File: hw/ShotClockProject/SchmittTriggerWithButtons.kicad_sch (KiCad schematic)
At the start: 10 parts, among them SW3 TK-6580S-2, SW4 TK-6580S-2, SW5 TK-6580S-2, U3 M74HC14YRM13TR

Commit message: Finished routing and added silk + part nmbr
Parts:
- C4: LCSC Part # C1525 -> (none)
- R31, R32, R33: LCSC Part # C25744 -> (none)
- SW3, SW4, SW5: LCSC Part # C528775 -> (none)
- U3: LCSC Part # C157450 -> (none)
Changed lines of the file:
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@@
       (effects (font (size 1.27 1.27)) (justify bottom) hide)
     )
-    (property "LCSC Part #" "C157450" (at 176.53 85.09 0)
+    (property "LCSC Part #" "" (at 176.53 85.09 0)
       (effects (font (size 1.27 1.27)) hide)
     )
@@
       (effects (font (size 1.27 1.27)) hide)
     )
-    (property "LCSC Part #" "C1525" (at 138.43 85.09 0)
+    (property "LCSC Part #" "" (at 138.43 85.09 0)
       (effects (font (size 1.27 1.27)) hide)
     )
@@
       (effects (font (size 1.27 1.27)) hide)
     )
-    (property "LCSC Part #" "C528775" (at 104.14 69.85 0)
+    (property "LCSC Part #" "" (at 104.14 69.85 0)
       (effects (font (size 1.27 1.27)) hide)
     )
@@
       (effects (font (size 1.27 1.27)) hide)
     )
-    (property "LCSC Part #" "C25744" (at 113.03 106.68 0)
+    (property "LCSC Part #" "" (at 113.03 106.68 0)
       (effects (font (size 1.27 1.27)) hide)
     )
@@
       (effects (font (size 1.27 1.27)) hide)
     )
-    (property "LCSC Part #" "C1525" (at 138.43 130.81 0)
+    (property "LCSC Part #" "" (at 138.43 130.81 0)
       (effects (font (size 1.27 1.27)) hide)
     )
@@
       (effects (font (size 1.27 1.27)) hide)
     )
-    (property "LCSC Part #" "C25744" (at 113.03 82.55 0)
+    (property "LCSC Part #" "" (at 113.03 82.55 0)
       (effects (font (size 1.27 1.27)) hide)
     )
@@
       (effects (font (size 1.27 1.27)) hide)
     )
-    (property "LCSC Part #" "C528775" (at 104.14 92.71 0)
+    (property "LCSC Part #" "" (at 104.14 92.71 0)
       (effects (font (size 1.27 1.27)) hide)
     )
@@
       (effects (font (size 1.27 1.27)) hide)
     )
-    (property "LCSC Part #" "C1525" (at 138.43 107.95 0)
+    (property "LCSC Part #" "" (at 138.43 107.95 0)
       (effects (font (size 1.27 1.27)) hide)
     )
@@
       (effects (font (size 1.27 1.27)) hide)
     )
-    (property "LCSC Part #" "C25744" (at 113.03 128.27 0)
+    (property "LCSC Part #" "" (at 113.03 128.27 0)
       (effects (font (size 1.27 1.27)) hide)
     )
@@
       (effects (font (size 1.27 1.27)) hide)
     )
-    (property "LCSC Part #" "C528775" (at 104.14 115.57 0)
-      (effects (font (size 1.27 1.27)) hide)
-    )
+    (property "LCSC Part #" "" (at 104.14 115.57 0)
+      (effects (font (size 1.27 1.27)) hide)
+    )

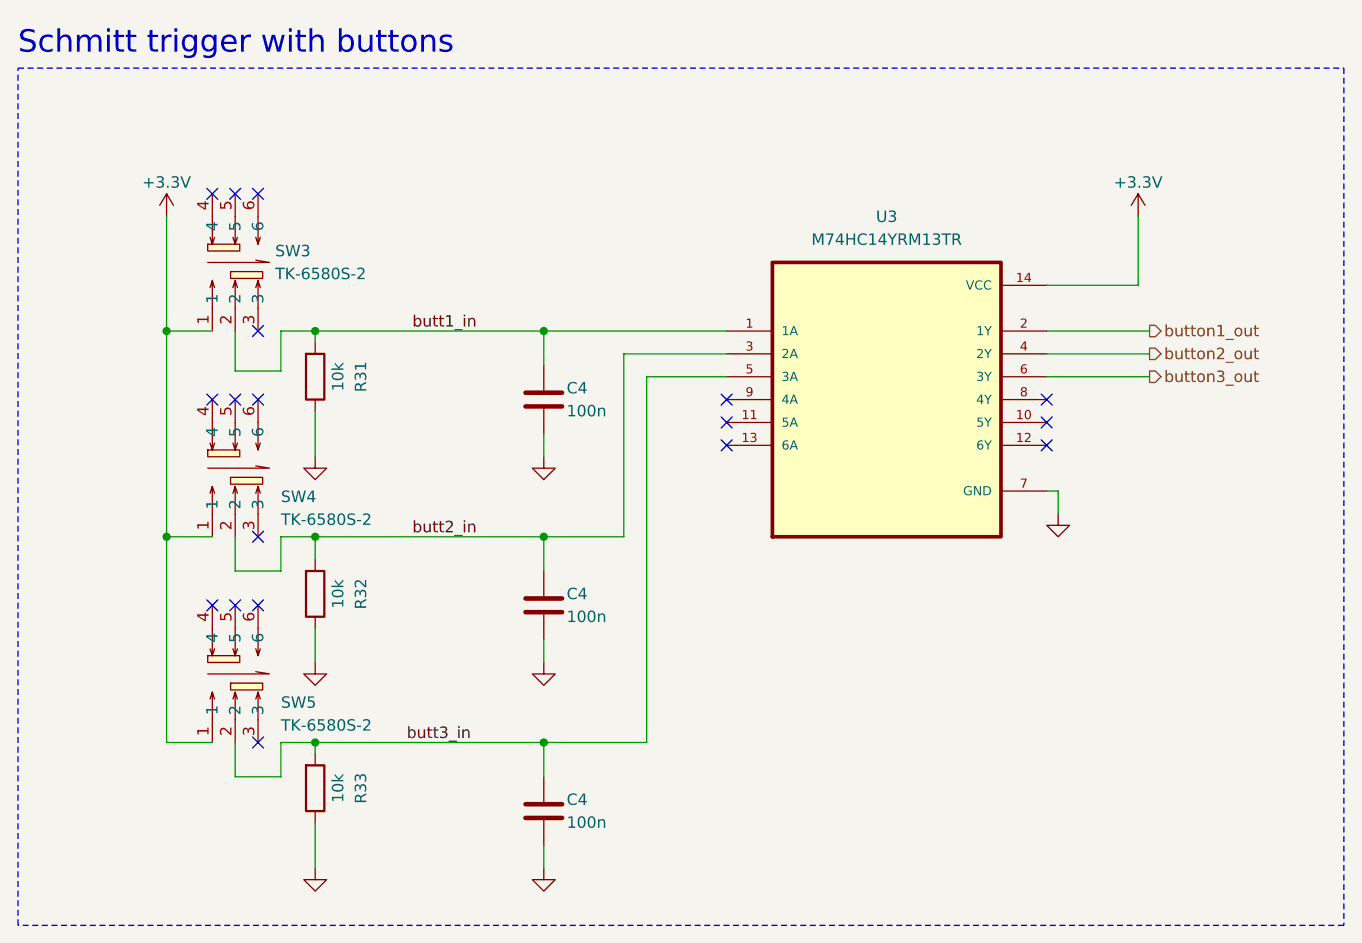
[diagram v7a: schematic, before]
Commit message: Add REV3 odt file, update CubeMX version and fix the ADC readout for battery voltage.
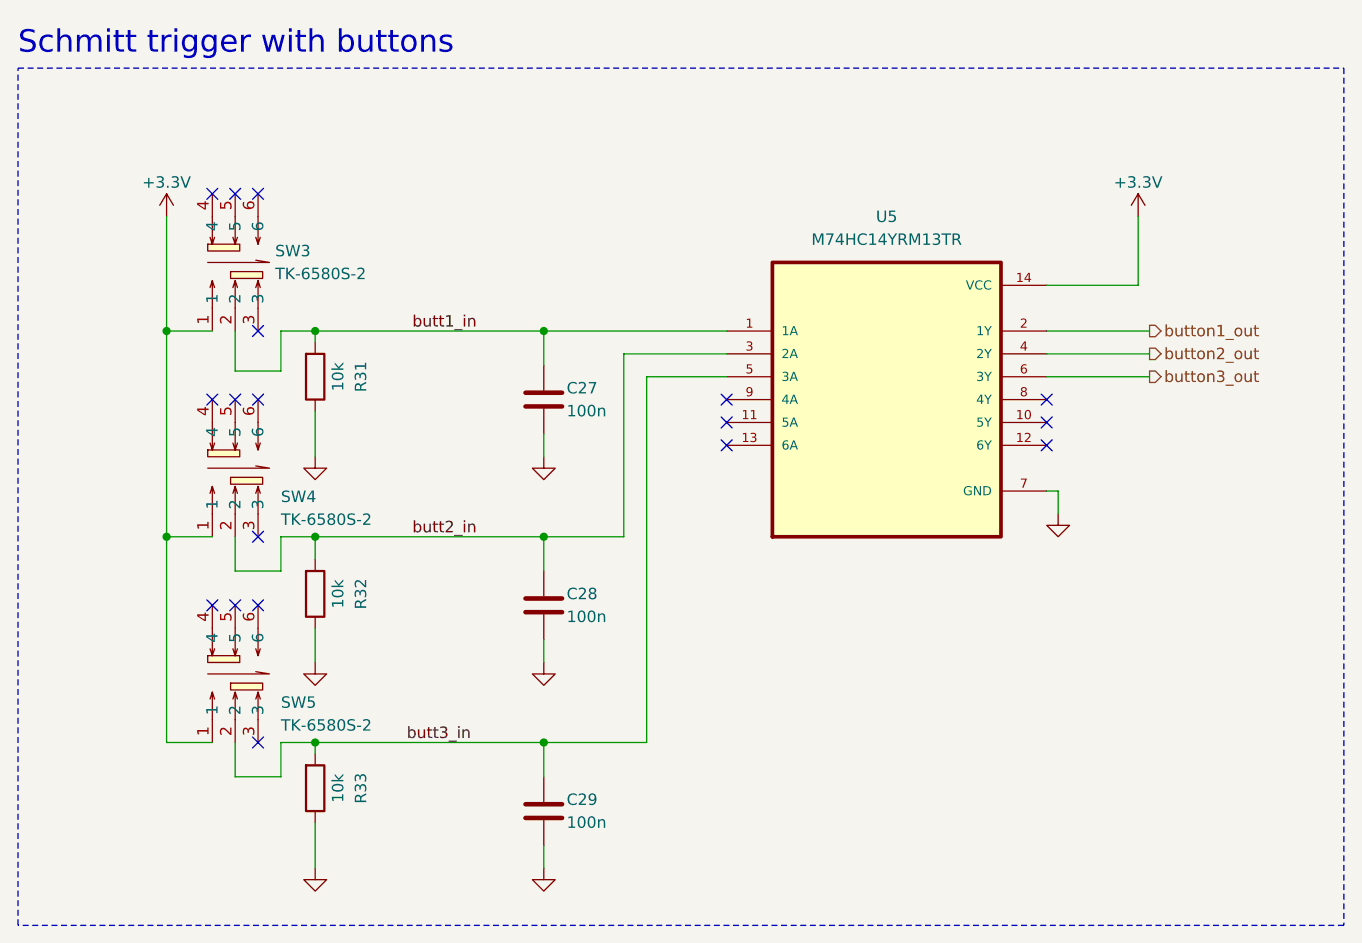
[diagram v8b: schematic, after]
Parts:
- renumbered C4 to C27, C4 to C28, C4 to C29, U3 to U5
